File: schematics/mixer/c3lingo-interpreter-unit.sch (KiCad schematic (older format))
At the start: 64 parts, among them J1 Headphone 1, J2 Mic 1, J3 Mix Line-Out, J4 Stage Line-In, J5 PowerSupply, SW1 Mute_1, SW2 OnAir_1, U1 LM833N, U2 NE5534, U3 LM833N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

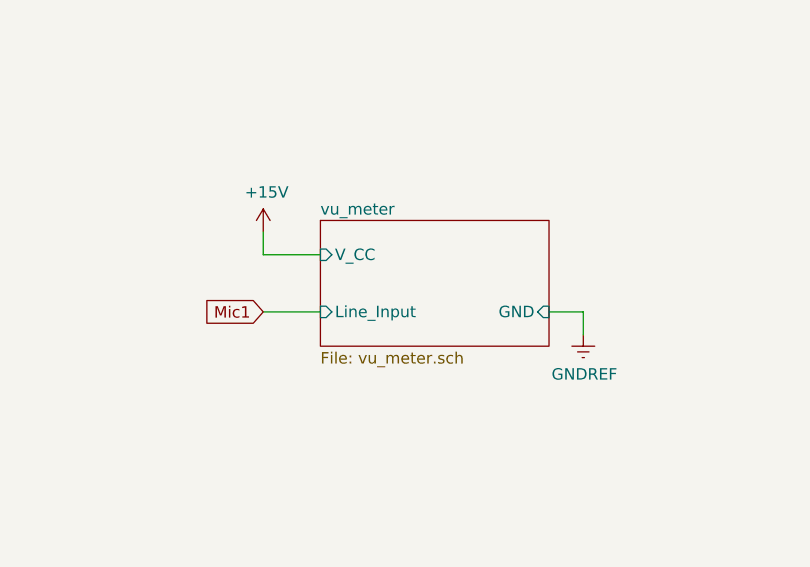
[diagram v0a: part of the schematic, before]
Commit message: Move VU-Meter to own project
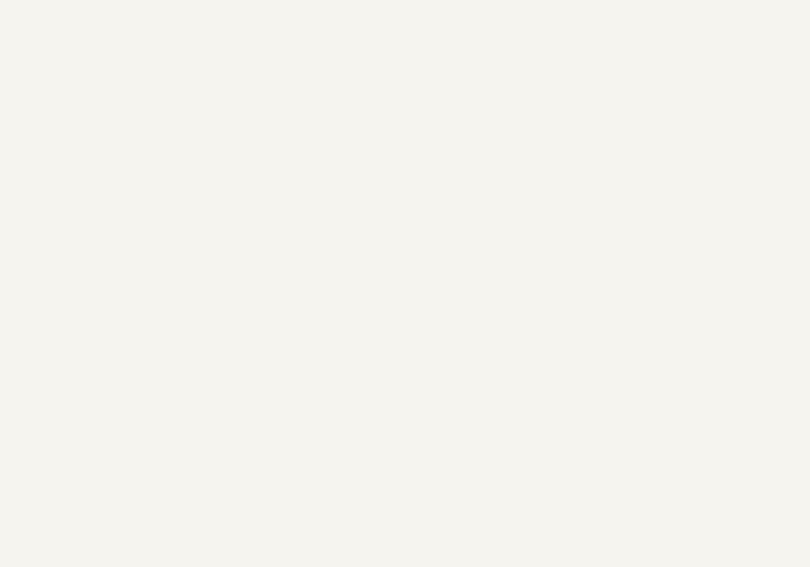
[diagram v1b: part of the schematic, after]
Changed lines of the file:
@@
 $Descr A3 16535 11693
 encoding utf-8
-Sheet 1 2
+Sheet 1 1
 Title ""
 Date ""
@@
 Wire Wire Line
 	14600 1800 14600 1900
-Text GLabel 9100 6550 0    50   Input ~ 0
-Mic1
 $Comp
 L Amplifier_Operational:LM358 U1
@@
 Text Notes 8600 650  0    50   ~ 0
 TODO: Rotation direction of potentiometers!\n(counter-clockwise less gain, clockwise more gain)
-$Sheet
-S 9350 6150 1000 550
-U 5FA7BAE6
-F0 "vu_meter" 50
-F1 "vu_meter.sch" 50
-F2 "V_CC" I L 9350 6300 50
-F3 "GND" I R 10350 6550 50
-F4 "Line_Input" I L 9350 6550 50
-$EndSheet
-$Comp
-L power:+15V #PWR037
-U 1 1 5FB63B06
-P 9100 6200
-F 0 "#PWR037" H 9100 6050 50  0001 C CNN
-F 1 "+15V" H 9115 6373 50  0000 C CNN
-F 2 "" H 9100 6200 50  0001 C CNN
-F 3 "" H 9100 6200 50  0001 C CNN
-	1    9100 6200
-	1    0    0    -1
-$EndComp
-$Comp
-L power:GNDREF #PWR038
-U 1 1 5FB64ECD
-P 10500 6650
-F 0 "#PWR038" H 10500 6400 50  0001 C CNN
-F 1 "GNDREF" H 10505 6477 50  0000 C CNN
-F 2 "" H 10500 6650 50  0001 C CNN
-F 3 "" H 10500 6650 50  0001 C CNN
-	1    10500 6650
-	1    0    0    -1
-$EndComp
-Wire Wire Line
-	10350 6550 10500 6550
-Wire Wire Line
-	10500 6550 10500 6650
 $Comp
 L power:GNDREF #PWR036
@@
 Wire Wire Line
 	6000 9100 6000 8850
-Wire Wire Line
-	9100 6550 9350 6550
 NoConn ~ 2850 1700
 NoConn ~ 12250 2000
@@
 Connection ~ 2650 1100
 Wire Wire Line
-	9100 6200 9100 6300
-Wire Wire Line
-	9100 6300 9350 6300
-Wire Wire Line
 	2650 800  2650 950

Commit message: Schematic Main: Add corrected headphone amp
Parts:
- added C22: 100nF, Capacitor_THT:C_Disc_D5.0mm_W2.5mm_P5.00mm, symbol Device:C
- added C23: 100uF, Capacitor_THT:CP_Radial_D10.0mm_P5.00mm, symbol Device:CP
- added C24: 220uF, Capacitor_THT:CP_Radial_D10.0mm_P5.00mm, symbol Device:CP
- added C26: 47nF, Capacitor_THT:C_Disc_D5.0mm_W2.5mm_P5.00mm, symbol Device:C
- added R24: R, Resistor_THT:R_Axial_DIN0207_L6.3mm_D2.5mm_P10.16mm_Horizontal, symbol Device:R
- added R25: 12R, Resistor_THT:R_Axial_DIN0207_L6.3mm_D2.5mm_P10.16mm_Horizontal, symbol Device:R
- added RV2: 25K, Potentiometer_THT:Potentiometer_Vishay_148-149_Single_Horizontal, symbol Device:R_POT
- added U7: LM386N-4, Package_DIP:DIP-8_W7.62mm_Socket_LongPads, symbol Amplifier_Audio:LM386
- C21: value 10uF -> 100uF
- R26: value 120R -> 220R
- R6: value 120R -> 820R
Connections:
- net +15V: now also C21.1, C22.2, U7.6 (V+)
- net GNDREF: now also C21.2, C22.1, C23.2, R25.2, RV2.1, U7.2 (-), U7.4 (GND)
- net Head1: now also R24.1
- net at J1.R, J1.T: now also C24.2
- net at R6.1: now also C25.2, R26.2, SW1.1, U1.2 (-); no longer C21.1
- new net: RV2.2, U7.3 (+)
- new net: C24.1, C26.1, U7.5
- new net: C23.1, U7.7 (BYPASS)
- new net: C26.2, R25.1
- new net: R24.2, RV2.3
- no-connect marks 13 -> 11
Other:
- note added: "Adjustable Input Gain\nGain: -11 to 30 dB\nGain = (220 + R_pot) / 820"
- note added: "HP Filter?\nf_c = 2.8 Hz\nTODO: Try 100 nF\nfor 300 Hz\n\nf_c = 1/(2*PI*R*C)"
- note added: "Headphone driver\nGain: 26 dB (20)"
- note added: "Summing Module\nGain: 0 dB"
- note added: "TODO: Check LP Filter Characteristic\n(see input module circuit)"
- note added: "TODO: Check capacitor value\nand if R8 is needed"
- note added: "TODO: On-Air button LEDs\n(actually one rd, one gn,\nwith common anode)"
- note added: "TODO: Try 10K or 100K poti\nwith matching feedback R\n(Keep LP filter in mind!)"
- note removed: "Headphone gain either at mix (summing)\nor at the driver"
- note removed: "Second Gain Stage\nGain: 0 to 48.6 dB\nGain = (120 + R_pot) / 120"
- note removed: "Summing Module\nGain: 0 dB\nIf feedback res. is variable,\ngain can be -inf to 0 dB"
- note removed: "TODO Headphone driver\nGain: TODO"
- note removed: "TODO: On-Air buttons"
- note removed: "TODO: Rotation direction of potentiometers!\n(counter-clockwise less gain, clockwise more gain)"
- note removed: "TODO: Try 10K or 100K poti\nwith matching feedback R"
- moved on the sheet: R6

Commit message: Refine headphone mix requirements, fix signal flow
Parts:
- added J6, J7: PowerSupply, TerminalBlock_MetzConnect:TerminalBlock_MetzConnect_Type073_RT02603HBLU_1x03_P5.08mm_Horizontal, symbol Connector:Conn_01x03_Male
- added RV15: 22K, Connector_PinHeader_2.54mm:PinHeader_2x03_P2.54mm_Vertical, symbol Device:R_POT_Dual
- added TP1, TP3, TP9: Mic1, TestPoint:TestPoint_THTPad_D2.0mm_Drill1.0mm, symbol Connector:TestPoint
- added TP10, TP4: Mic2, TestPoint:TestPoint_THTPad_D2.0mm_Drill1.0mm, symbol Connector:TestPoint
- added TP11, TP5: Mic3, TestPoint:TestPoint_THTPad_D2.0mm_Drill1.0mm, symbol Connector:TestPoint
- added TP2, TP8: Stage, TestPoint:TestPoint_THTPad_D2.0mm_Drill1.0mm, symbol Connector:TestPoint
- added TP6, TP7: MicSum, TestPoint:TestPoint_THTPad_D2.0mm_Drill1.0mm, symbol Connector:TestPoint
- C6: footprint Capacitor_THT:CP_Radial_D10.0mm_P5.00mm -> Capacitor_THT:CP_Radial_D5.0mm_P2.50mm
- R24: value R -> 82K
- renumbered R27 to RV11, R3 to RV13, R4 to RV14, RV2 to RV19
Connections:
- net +15V: now also J6.1 (Pin_1), J7.1 (Pin_1)
- net -15V: now also J6.3 (Pin_3), J7.3 (Pin_3)
- net GNDREF: now also RV13.1, J6.2 (Pin_2), J7.2 (Pin_2), RV15.1, RV15.4
- net Mic1: now also RV14.3, TP1.1, TP3.1, TP9.1
- net MicSum: now also TP6.1, TP7.1; no longer RV14.3
- net Stage: now also RV13.3, TP2.1, TP8.1; no longer R9.2
- net at R14.2: now also TP10.1
- net at R16.2: now also TP11.1
- net at C3.2, RV14.2, U1.6 (-): now also R9.2, RV13.2, RV15.2, RV15.5; no longer R9.1, RV13.1
- net at C3.1, C7.2, U1.7: now also R9.1; no longer RV13.2
- new net: RV15.6, TP4.1
- new net: RV15.3, TP5.1
- no-connect marks 11 -> 8
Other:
- note added: "HP Filter?\nf_c = 2.8 Hz\nTODO: Try 47R\nfor 300 Hz\n\nf_c = 1/(2*PI*R*C)"
- note added: "Mic2"
- note added: "Mic3"
- note removed: "HP Filter?\nf_c = 2.8 Hz\nTODO: Try 100 nF\nfor 300 Hz\n\nf_c = 1/(2*PI*R*C)"
- moved on the sheet: R9, RV13, RV14

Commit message: final fixes for first prototype PCB order
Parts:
- added C27: 220p, Capacitor_THT:C_Disc_D5.0mm_W2.5mm_P5.00mm, symbol Device:C
- added R3: 10K, Resistor_THT:R_Axial_DIN0207_L6.3mm_D2.5mm_P10.16mm_Horizontal, symbol Device:R
- added R4: 3.3K, Resistor_THT:R_Axial_DIN0207_L6.3mm_D2.5mm_P10.16mm_Horizontal, symbol Device:R
- C7: value 10nF -> 100nF
- R17, R18, R21, R23: value R -> 10K
- R24: value 82K -> 820K
- R8: value 47R -> 10K
- RV1, RV11, RV13, RV14, RV15, RV19: Notes (none) -> Model 95 has solder lugs
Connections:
- net at R21.1, R23.1: now also U4.3 (+); no longer U4.2 (-)
- net at R17.2, R18.1: now also U4.2 (-); no longer U4.3 (+)
- net at R18.2: now also C27.1, R3.2; no longer JP1.1 (A)
- net at R21.2: now also R8.2, C27.2; no longer JP2.1 (A)
- net at U7.3 (+): now also C7.1; no longer RV19.2
- net at C3.1, R9.1, U1.7: now also R24.1; no longer C7.2
- net Head1: no longer names the net of R8.1
- net Head1: now also JP2.1 (A), R4.1; no longer R24.1
- new net: C7.2, RV19.2
- new net: JP1.1 (A), R3.1, R4.2
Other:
- note added: "Balanced Line Input Converter\nGain: 1\n220pF for HF rolloff (20 kHz)"
- note added: "HP Filter?\nTODO: Try 120R\nfor ca. 150 Hz\n\nf_c = 1/(2*PI*R*C)"
- note added: "TODO: use INA134 **or** own design"
- note added: "TODO:\nLog./ Lin.?"
- note removed: "Balanced Converter\nGain: 0 dB\nTODO: use INA134?"
- note removed: "HP Filter?\nf_c = 2.8 Hz\nTODO: Try 47R\nfor 300 Hz\n\nf_c = 1/(2*PI*R*C)"
- note removed: "TODO: Check LP Filter Characteristic\n(see input module circuit)"
- note removed: "TODO: Check capacitor value\nand if R8 is needed"
- moved on the sheet: C11, C12, C14, C15, C16, C17, C18, C25, C3, C4, C5, C7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

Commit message: Main: Summing design flaw fixed; better headphone vol. range
- Multiple R and C value adaptions
- Line Input: No relevant difference between INA134 and own circuit -> LM833 chosen
- Signal busses/ summing module inputs fixed
- TODO: On-Air Button
- TODO: Update PCB layout
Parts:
- removed C13: 4.7pF, Capacitor_THT:C_Disc_D5.0mm_W2.5mm_P5.00mm, symbol Device:C
- removed C19, C20: 1uF, Capacitor_THT:C_Disc_D5.0mm_W2.5mm_P5.00mm, symbol Device:C
- removed J7: PowerSupply, TerminalBlock_MetzConnect:TerminalBlock_MetzConnect_Type073_RT02603HBLU_1x03_P5.08mm_Horizontal, symbol Connector:Conn_01x03_Male
- removed JP1: Stage Hot, Connector_PinHeader_2.54mm:PinHeader_1x03_P2.54mm_Vertical, symbol Jumper:Jumper_3_Bridged12
- removed JP2: Stage Cold, Connector_PinHeader_2.54mm:PinHeader_1x03_P2.54mm_Vertical, symbol Jumper:Jumper_3_Bridged12
- removed JP3: Stage Out, Connector_PinHeader_2.54mm:PinHeader_1x03_P2.54mm_Vertical, symbol Jumper:Jumper_3_Bridged12
- removed R15: 47R, Resistor_THT:R_Axial_DIN0207_L6.3mm_D2.5mm_P10.16mm_Horizontal, symbol Device:R
- removed R22: 22K, Resistor_THT:R_Axial_DIN0207_L6.3mm_D2.5mm_P10.16mm_Horizontal, symbol Device:R
- removed TP7: MicSum, TestPoint:TestPoint_THTPad_D2.0mm_Drill1.0mm, symbol Connector:TestPoint
- removed U6: INA134PA, Package_DIP:DIP-8_W7.62mm_Socket_LongPads, symbol JBeyerstedt-Library:INA134PA
- added R27: 2.2K, Resistor_THT:R_Axial_DIN0207_L6.3mm_D2.5mm_P10.16mm_Horizontal, symbol Device:R
- added R28, R29, R30, R31: 22K, Resistor_THT:R_Axial_DIN0207_L6.3mm_D2.5mm_P10.16mm_Horizontal, symbol Device:R
- C1, C21, C23, C9: Model (none) -> 25V
- C24: footprint Capacitor_THT:CP_Radial_D10.0mm_P5.00mm -> Capacitor_THT:CP_Radial_D6.3mm_P2.50mm; Model (none) -> 16V low ESR
- C25: value 0.1uF -> 100nF
- C27: value 220p -> 220pF
- C6: value 10uF -> 1uF; footprint Capacitor_THT:CP_Radial_D5.0mm_P2.50mm -> Capacitor_THT:CP_Radial_D5.0mm_P2.00mm; Model (none) -> 16V low ESR electrolytic // plastic film
- C7: value 100nF -> 1uF; footprint Capacitor_THT:C_Disc_D5.0mm_W2.5mm_P5.00mm -> Capacitor_THT:CP_Radial_D5.0mm_P2.00mm; symbol Device:C -> Device:CP; Model (none) -> 16V low ESR electrolytic // plastic film
- J1: Model (none) -> 6.3 mm Jack (female)
- J2: Model (none) -> XLR (female)
- J3: Model (none) -> XLR (male)
- J4: Model (none) -> Combo XLR + 6.3 mm Jack
- R24: value 820K -> 330K
- R26: value 220R -> 270R
- R6: value 820R -> 1.5K
- R7: value 5.6K -> 470R
- RV1: footprint Potentiometer_THT:Potentiometer_Vishay_148-149_Single_Horizontal -> Potentiometer_THT:Potentiometer_Vishay_T73XX_Horizontal; Model (none) -> Vishay M64{Y,Z}104; Notes Model 95 has solder lugs -> (none)
- RV11, RV19: value 25K -> 50K log.; footprint Potentiometer_THT:Potentiometer_Vishay_148-149_Single_Horizontal -> JBeyerstedt-Library:Potentiometer_Alps_RK11K_Single_Horizontal; Model (none) -> Alps RK11K1120-A503; Notes Model 95 has solder lugs -> (none)
- RV13, RV14: value 22K -> 50K log.; footprint Potentiometer_THT:Potentiometer_Vishay_148-149_Single_Horizontal -> JBeyerstedt-Library:Potentiometer_Alps_RK11K_Single_Horizontal; Model (none) -> Alps RK11K1120-A503; Notes Model 95 has solder lugs -> (none)
- RV15: value 22K -> 50K log. st.; footprint Connector_PinHeader_2.54mm:PinHeader_2x03_P2.54mm_Vertical -> Potentiometer_THT:Potentiometer_Alps_RK09L_Double_Horizontal; Model (none) -> Alps RK14K12B0A0R / RK09L1220; Notes Model 95 has solder lugs -> (none)
- SW2: Model (none) -> E-Switch TODO
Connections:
- net MicSum is gone; now on an unnamed net: TP6.1, U5.4 (VIN)
- net GNDREF: now also R27.2; no longer RV19.1
- net at R17.1, U4.1: now also R20.2
- net at J4.3, J4.R: now also R4.1, R8.1
- net at J4.2, J4.T: now also R3.1, R4.2
- net at U7.3 (+): now also C7.2; no longer C7.1
- net at RV19.2: now also C7.1; no longer C7.2
- new net: R27.1, RV19.1
- new net: R31.2, RV15.2
- new net: R30.2, RV15.5
- new net: C3.2, R28.1, R29.1, R30.1, R31.1, R9.2, U1.6 (-)
- new net: R28.2, RV13.2
- new net: R29.2, RV14.2
- no-connect marks 8 -> 7
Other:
- note added: "Adjustable Input Gain\nGain: -15 to 30 dB"
- note added: "HP Filter 350 Hz\nf_c = 1/(2*PI*R*C)"
- note added: "Summing Module\nGain: -inf to 0 dB per Ch."
- note added: "TODO: Add 15 V phantom power\nfor Superlux headset"
- note added: "TODO: C at pin 7 has\nno audible effect"
- note removed: "Adjustable Input Gain\nGain: -11 to 30 dB\nGain = (220 + R_pot) / 820"
- note removed: "HP Filter?\nTODO: Try 120R\nfor ca. 150 Hz\n\nf_c = 1/(2*PI*R*C)"
- note removed: "Summing Module\nGain: -inf to 0 dB"
- note removed: "TODO: Try 10K or 100K poti\nwith matching feedback R\n(Keep LP filter in mind!)"
- note removed: "TODO: use INA134 **or** own design"
- note removed: "TODO:\nLog./ Lin.?"
- moved on the sheet: C10, C11, C12, C14, C15, C16, C17, C18, C21, C22, C23, C24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

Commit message: Main: Add 15V phantom power
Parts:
- added C13, C20: 1uF, Capacitor_THT:CP_Radial_D5.0mm_P2.00mm, symbol Device:CP
- added C19: 100uF, Capacitor_THT:CP_Radial_D10.0mm_P5.00mm, symbol Device:CP
- added D1, D2, D3, D4: 1N4148, Diode_THT:D_DO-35_SOD27_P10.16mm_Horizontal, symbol Device:D
- added R15, R22: 680R 1%, Resistor_THT:R_Axial_DIN0207_L6.3mm_D2.5mm_P10.16mm_Horizontal, symbol Device:R
- SW1: Model (none) -> NKK Switches UB15{NBK,NK}{W,G}{01,03}N-C
- SW2: Model E-Switch TODO -> E-Switch LP11EE1NCSYG
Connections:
- net +15V: now also C19.1, R15.2, R22.1
- net at J2.2: now also C13.1, R15.1; no longer R1.2
- net at J2.3: now also C20.1, R22.2; no longer R10.2
- net GNDREF renamed GND
- net GND: now also C19.2, D1.1 (K), D2.2 (A), D3.1 (K), D4.2 (A)
- new net: C13.2, D1.2 (A), D2.1 (K), R1.2
- new net: C20.2, D3.2 (A), D4.1 (K), R10.2
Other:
- note added: "Phantom Power\n(15V)"
- note removed: "TODO: Add 15 V phantom power\nfor Superlux headset"
- moved on the sheet: C1, C2, C25, C4, C5, C6, C8, C9, R1, R10, R11, R2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
